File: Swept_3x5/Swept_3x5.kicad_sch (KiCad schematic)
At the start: 82 parts, among them SW10 SW_Push, SW10_r1 SW_Push, SW11 SW_Push, SW11_r1 SW_Push, SW12 SW_Push, SW12_r1 SW_Push, SW13 SW_Push, SW13_r1 SW_Push, SW15 SW_Push, SW15_r1 SW_Push, SW16 SW_Push, SW16_r1 SW_Push, SW17 SW_Push, SW17_r1 SW_Push, SW18 SW_Push, SW18_r1 SW_Push, SW19 SW_Push, SW19_r1 SW_Push, SW20 SW_Push, SW20_r1 SW_Push, SW21 SW_Push, SW21_r1 SW_Push, SW22 SW_Push, SW22_r1 SW_Push, SW3 SW_Push, SW3_r1 SW_Push, SW4 SW_Push, SW4_r1 SW_Push, SW5 SW_Push, SW5_r1 SW_Push, SW6 SW_Push, SW6_r1 SW_Push, SW7 SW_Push, SW7_r1 SW_Push, SW9 SW_Push, SW9_r1 SW_Push, U1 ProMicro-kbd, U2 ProMicro-kbd

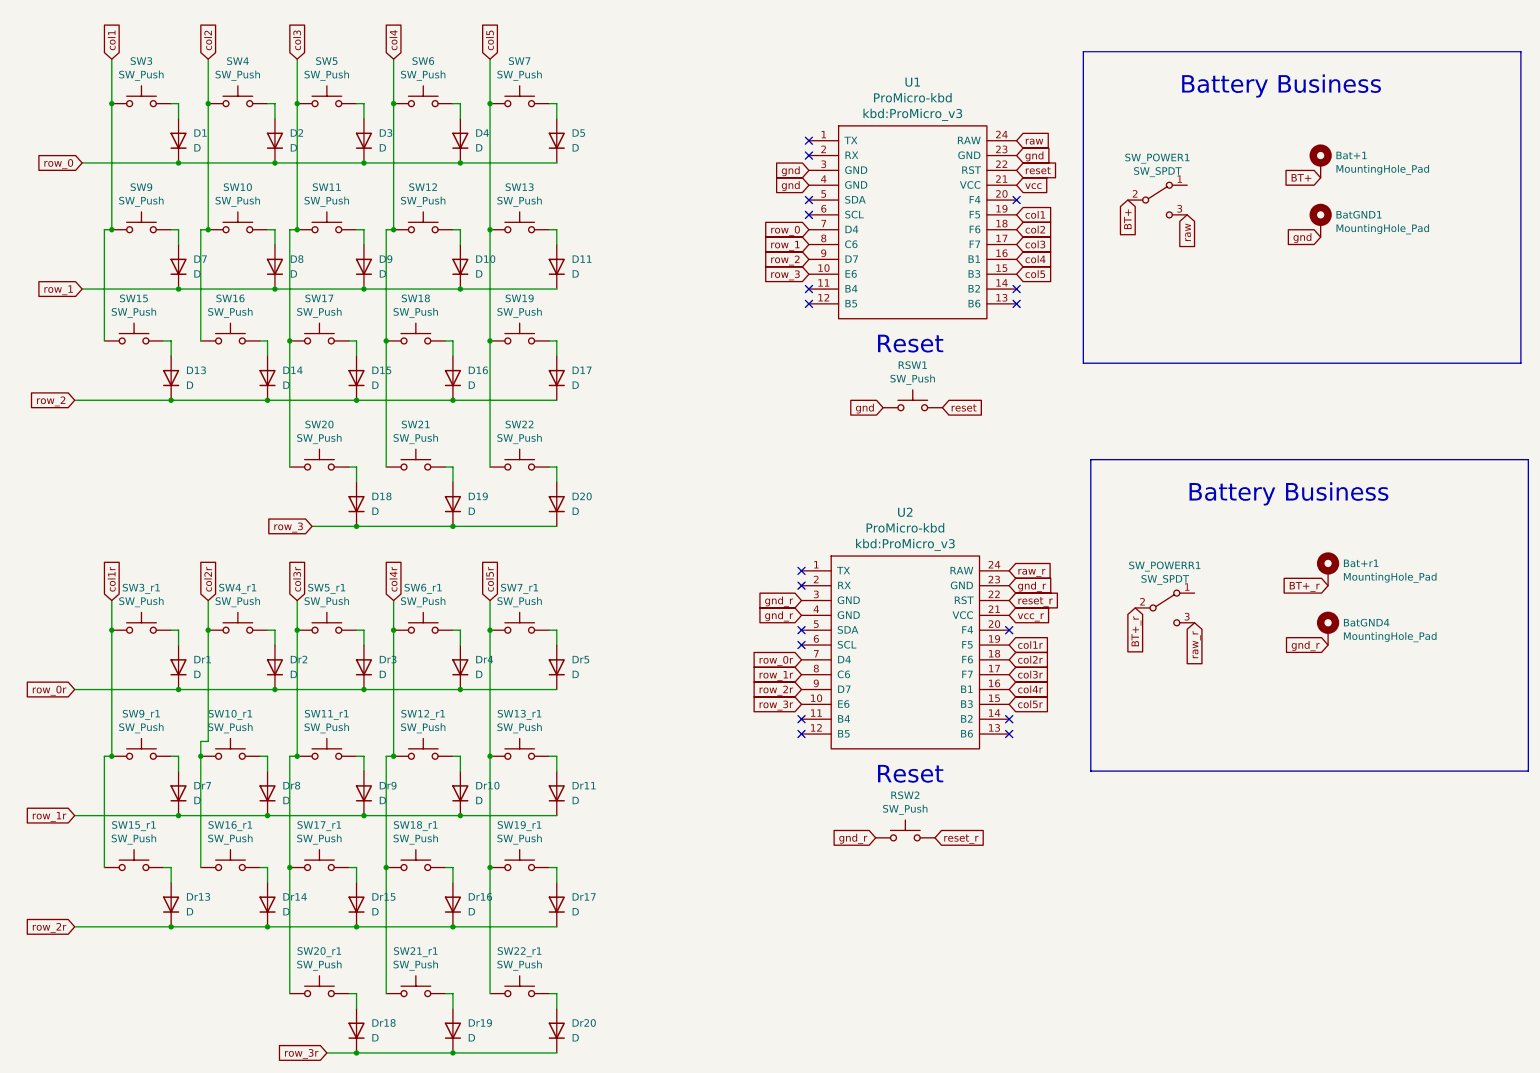
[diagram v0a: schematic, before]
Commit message: Added support for Kailh hot-swap sockets.
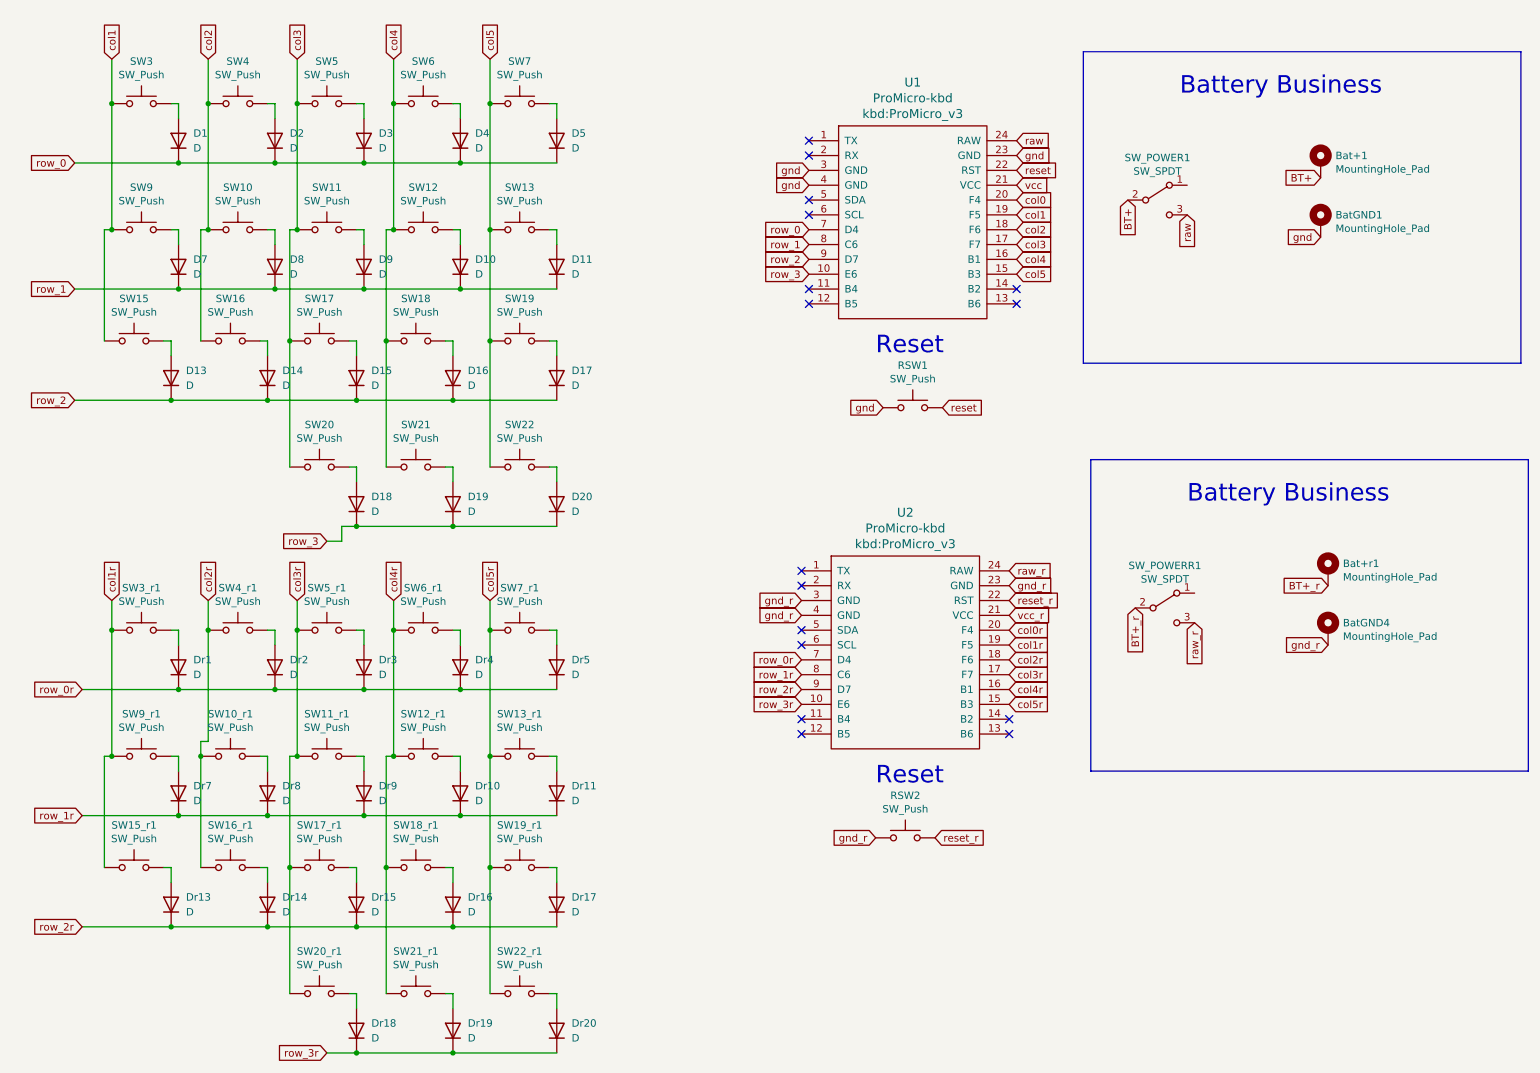
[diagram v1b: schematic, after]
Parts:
- D1, D10, D11, D13, D14, D15, D16, D17, D18, D19, D2, D20, D3, D4, D5, D7, D8, D9, Dr1, Dr10, Dr11, Dr13, Dr14, Dr15, Dr16, Dr17, Dr18, Dr19, Dr2, Dr20, Dr3, Dr4, Dr5, Dr7, Dr8, Dr9: LCSC (none) -> C2099
- SW10, SW10_r1, SW11, SW11_r1, SW12, SW12_r1, SW13, SW13_r1, SW15, SW15_r1, SW16, SW16_r1, SW17, SW17_r1, SW18, SW18_r1, SW19, SW19_r1, SW20, SW20_r1, SW21, SW21_r1, SW22, SW22_r1, SW3, SW3_r1, SW4, SW4_r1, SW5, SW5_r1, SW6, SW6_r1, SW7, SW7_r1, SW9, SW9_r1: footprint aym1607:choc-v1-with-millmax -> keyswitches:Kailh_socket_PG1350_optional
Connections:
- net col0: now reaches U1.20 (F4)
- net col0r: now reaches U2.20 (F4)
- no-connect marks 18 -> 16

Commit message: Added nice!view support for 3x5
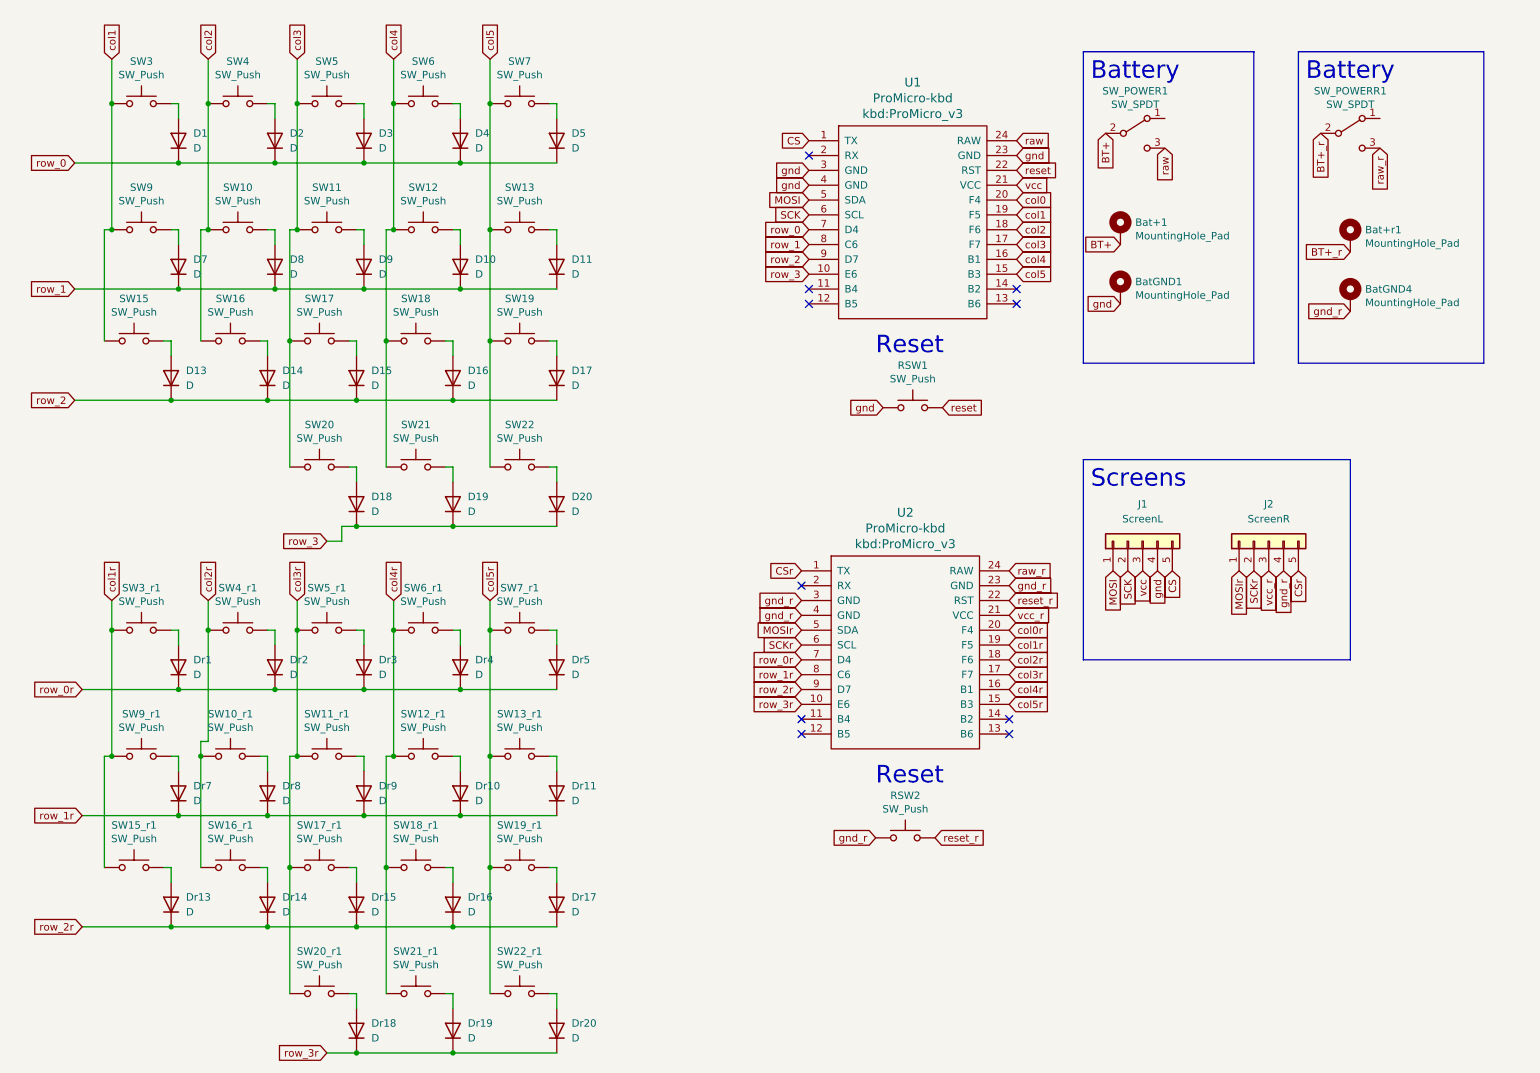
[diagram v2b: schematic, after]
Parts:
- added J1: ScreenL, Connector_PinHeader_2.54mm:PinHeader_1x05_P2.54mm_Vertical, symbol Connector_Generic:Conn_01x05
- added J2: ScreenR, Connector_PinHeader_2.54mm:PinHeader_1x05_P2.54mm_Vertical, symbol Connector_Generic:Conn_01x05
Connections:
- net gnd: now also J1.4 (Pin_4)
- net gnd_r: now also J2.4 (Pin_4)
- net vcc: now also J1.3 (Pin_3)
- net vcc_r: now also J2.3 (Pin_3)
- net CS: now reaches U1.1 (TX)
- net CS: now also J1.5 (Pin_5)
- net MOSI: now reaches U1.5 (SDA)
- net MOSI: now also J1.1 (Pin_1)
- net SCK: now reaches U1.6 (SCL)
- net SCK: now also J1.2 (Pin_2)
- net CSr: now reaches U2.1 (TX)
- net CSr: now also J2.5 (Pin_5)
- net MOSIr: now reaches U2.5 (SDA)
- net MOSIr: now also J2.1 (Pin_1)
- net SCKr: now reaches U2.6 (SCL)
- net SCKr: now also J2.2 (Pin_2)
- no-connect marks 16 -> 10
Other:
- note added: "Battery"
- note added: "Screens"
- note removed: "Battery Business"
- moved on the sheet: Bat+1, Bat+r1, BatGND1, BatGND4, SW_POWER1, SW_POWERR1
